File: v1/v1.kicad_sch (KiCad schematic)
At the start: 59 parts, among them CON1 SNES-CONN

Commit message: v1: fixed /WRAM vs CPU_CLK jumper selector to make sense; lots of PCB routing decisions
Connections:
- net CPU_CLK: now also JP3.3 (B); no longer JP3.2 (C)
- net ~{WRAM}: now also JP3.1 (A); no longer JP3.3 (B)
- net at Pico1.27 (GP21): now also JP3.2 (C); no longer JP3.1 (A)
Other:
- moved on the sheet: JP3
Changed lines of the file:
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@@
     (stroke (width 0) (type default) (color 0 0 0 0))
   )
+  (wire (pts (xy 189.23 151.13) (xy 186.69 151.13))
+    (stroke (width 0) (type default) (color 0 0 0 0))
+  )
   (wire (pts (xy 266.7 25.4) (xy 266.7 29.21))
     (stroke (width 0) (type default) (color 0 0 0 0))
@@
     (stroke (width 0) (type default) (color 0 0 0 0))
   )
+  (wire (pts (xy 189.23 138.43) (xy 186.69 138.43))
+    (stroke (width 0) (type default) (color 0 0 0 0))
+  )
   (wire (pts (xy 218.44 26.67) (xy 218.44 29.21))
     (stroke (width 0) (type default) (color 0 0 0 0))
@@
     (effects (font (size 1.27 1.27)) (justify right bottom))
   )
-  (label "CPU_CLK" (at 189.23 140.97 90)
+  (label "CPU_CLK" (at 189.23 138.43 0)
     (effects (font (size 1.27 1.27)) (justify left bottom))
   )
@@
     (effects (font (size 1.27 1.27)) (justify right bottom))
   )
-  (label "~{WRAM}" (at 195.58 144.78 0)
+  (label "~{WRAM}" (at 189.23 151.13 0)
     (effects (font (size 1.27 1.27)) (justify left bottom))
   )
@@
     (pin "1")
   )
-  (symbol (lib_id "Jumper:Jumper_3_Open") (at 189.23 144.78 0) (mirror x) (unit 1)
+  (symbol (lib_id "Jumper:Jumper_3_Open") (at 186.69 144.78 270) (mirror x) (unit 1)
     (in_bom yes) (on_board yes)
-    (property "Reference" "JP3" (id 0) (at 189.23 148.59 0))
-    (property "Value" "CLK_OR_WRAM" (id 1) (at 189.23 148.59 0)
+    (property "Reference" "JP3" (id 0) (at 190.5 144.78 0))
+    (property "Value" "CLK_OR_WRAM" (id 1) (at 190.5 144.78 0)
       (effects (font (size 1.27 1.27)) hide)
     )
-    (property "Footprint" "Connector_PinHeader_2.54mm:PinHeader_1x03_P2.54mm_Vertical" (id 2) (at 189.23 144.78 0)
+    (property "Footprint" "Connector_PinHeader_2.54mm:PinHeader_1x03_P2.54mm_Vertical" (id 2) (at 186.69 144.78 0)
       (effects (font (size 1.27 1.27)) hide)
     )
-    (property "Datasheet" "~" (id 3) (at 189.23 144.78 0)
+    (property "Datasheet" "~" (id 3) (at 186.69 144.78 0)
       (effects (font (size 1.27 1.27)) hide)
     )

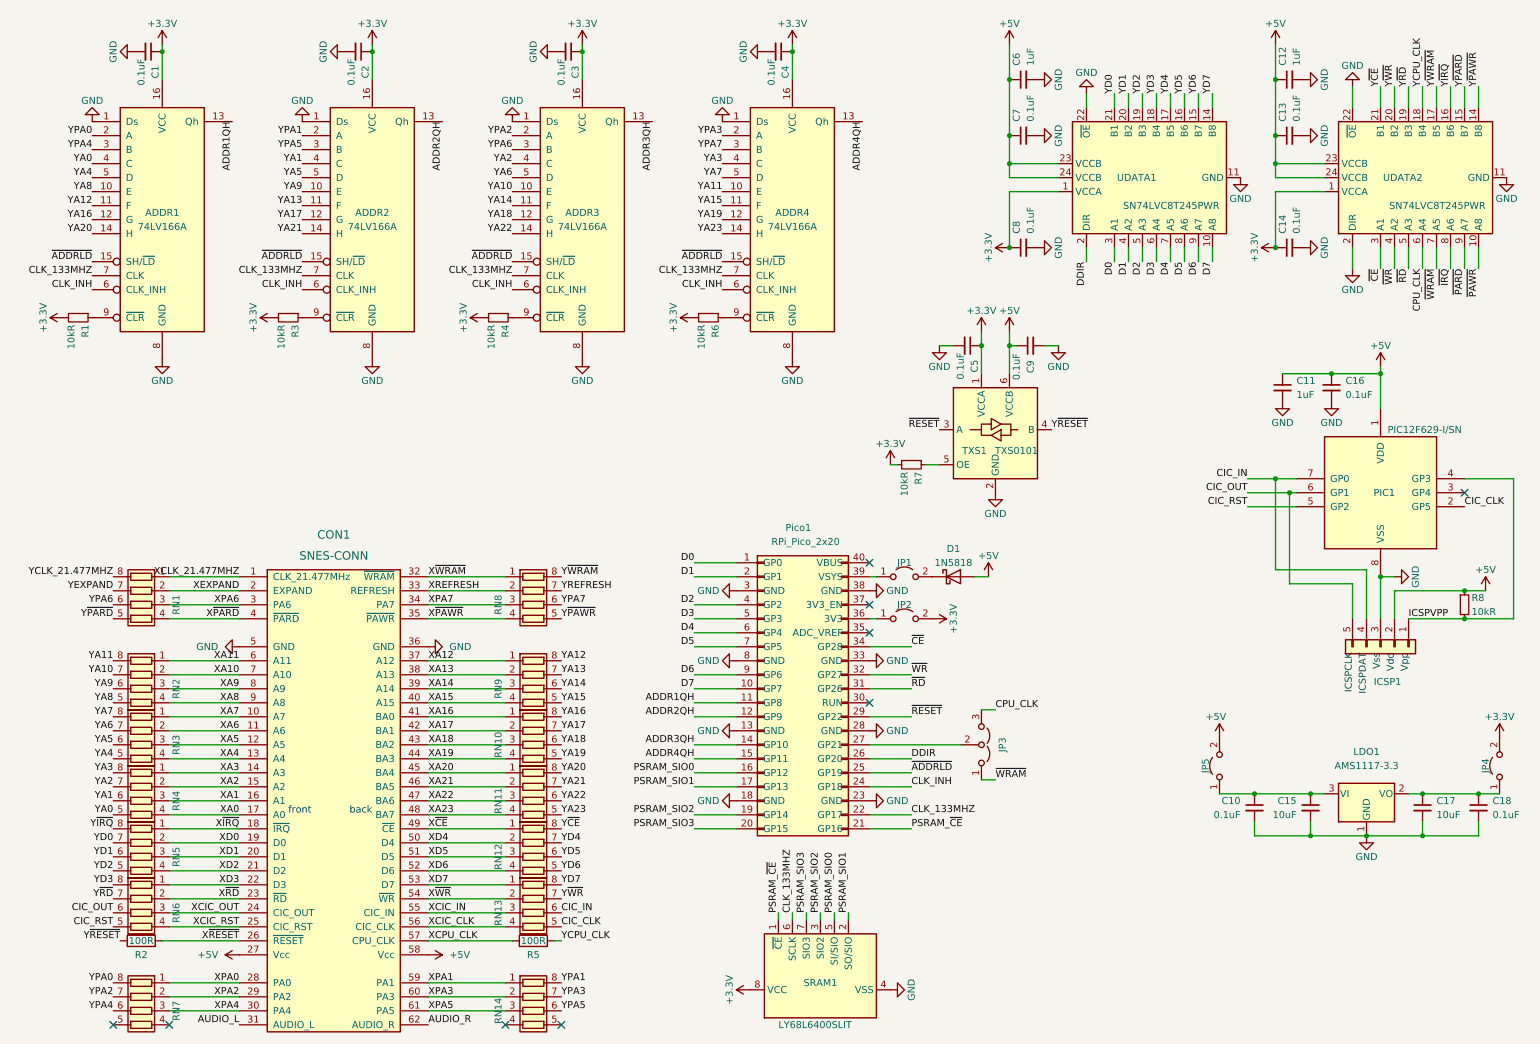
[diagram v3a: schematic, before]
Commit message: v1: lots of routing and better placement of components
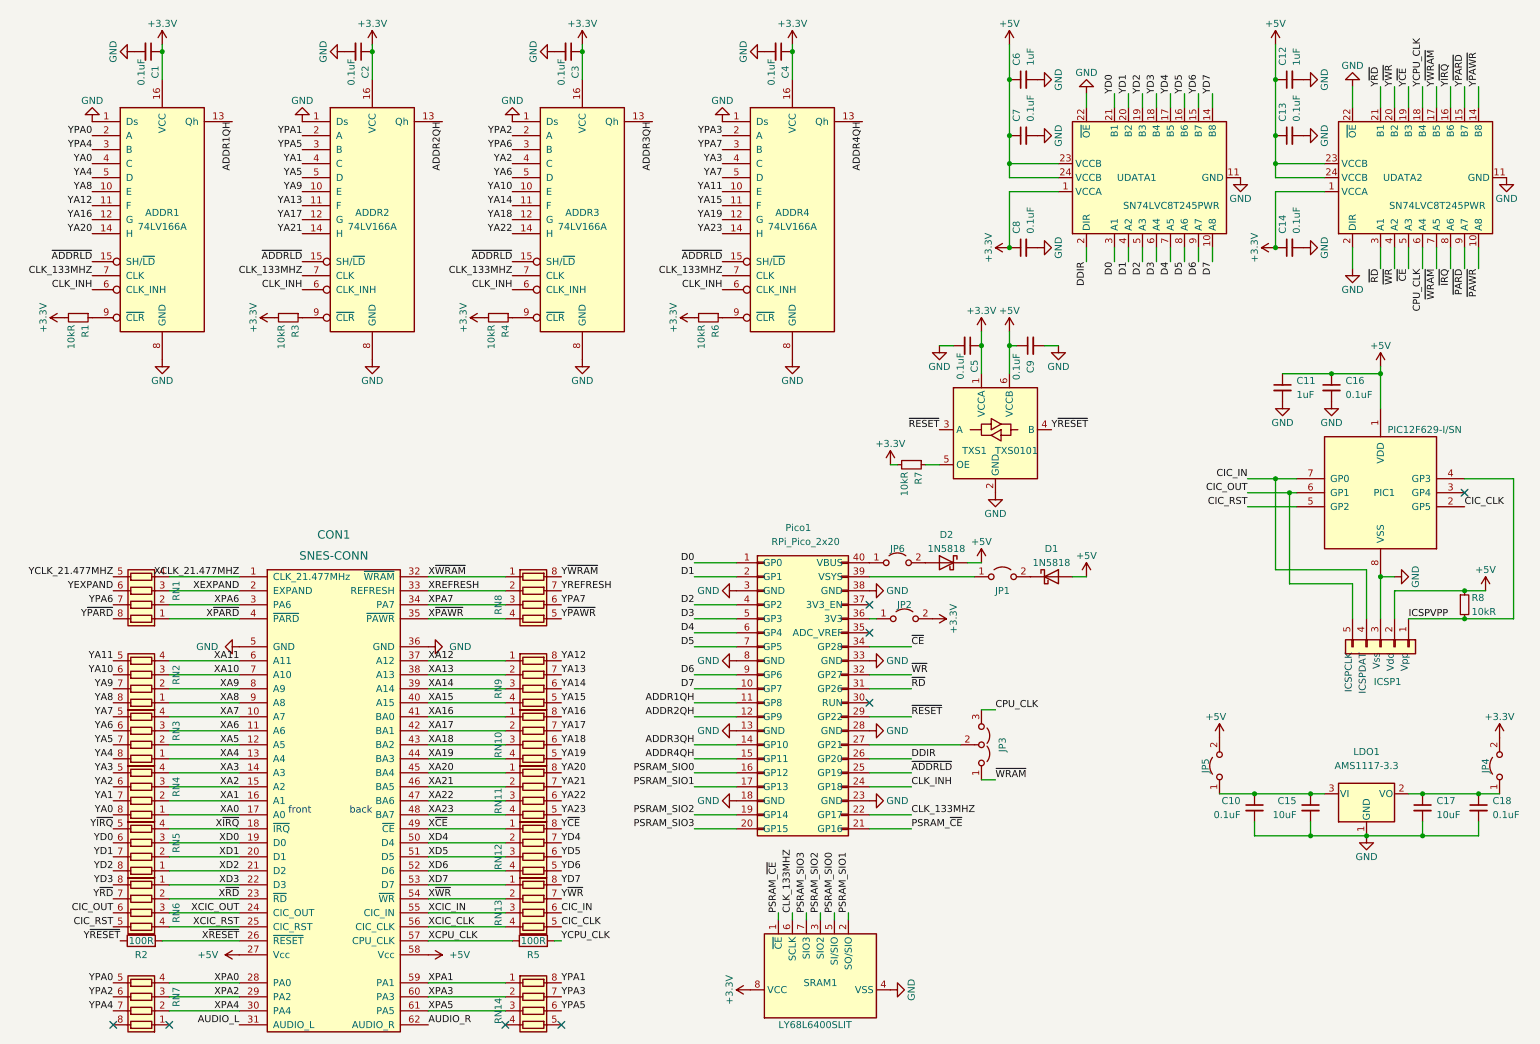
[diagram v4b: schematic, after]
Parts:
- added D2: 1N5818, Diode_THT:D_DO-41_SOD81_P7.62mm_Horizontal, symbol Diode:1N5818
- added JP6: PICO_5V_OUT, Connector_PinHeader_2.54mm:PinHeader_1x02_P2.54mm_Vertical, symbol Jumper:Jumper_2_Open
- JP1: value SNES 5V -> Pico -> PICO_5V_IN
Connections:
- net +5V: now also D2.1 (K)
- net XA0: now also RN4.1 (R1.1); no longer RN4.4 (R4.1)
- net XA1: now also RN4.2 (R2.1); no longer RN4.3 (R3.1)
- net XA10: now also RN2.3 (R3.1); no longer RN2.2 (R2.1)
- net XA11: now also RN2.4 (R4.1); no longer RN2.1 (R1.1)
- net XA2: now also RN4.3 (R3.1); no longer RN4.2 (R2.1)
- net XA3: now also RN4.4 (R4.1); no longer RN4.1 (R1.1)
- net XA4: now also RN3.1 (R1.1); no longer RN3.4 (R4.1)
- net XA5: now also RN3.2 (R2.1); no longer RN3.3 (R3.1)
- net XA6: now also RN3.3 (R3.1); no longer RN3.2 (R2.1)
- net XA7: now also RN3.4 (R4.1); no longer RN3.1 (R1.1)
- net XA8: now also RN2.1 (R1.1); no longer RN2.4 (R4.1)
- net XA9: now also RN2.2 (R2.1); no longer RN2.3 (R3.1)
- net XCLK_21.477MHZ: now also RN1.4 (R4.1); no longer RN1.1 (R1.1)
- net XD0: now also RN5.3 (R3.1); no longer RN5.2 (R2.1)
- net XD1: now also RN5.2 (R2.1); no longer RN5.3 (R3.1)
- net XD2: now also RN5.1 (R1.1); no longer RN5.4 (R4.1)
- net XEXPAND: now also RN1.3 (R3.1); no longer RN1.2 (R2.1)
- net XPA0: now also RN7.4 (R4.1); no longer RN7.1 (R1.1)
- net XPA2: now also RN7.3 (R3.1); no longer RN7.2 (R2.1)
- net XPA4: now also RN7.2 (R2.1); no longer RN7.3 (R3.1)
- net XPA6: now also RN1.2 (R2.1); no longer RN1.3 (R3.1)
- net X~{IRQ}: now also RN5.4 (R4.1); no longer RN5.1 (R1.1)
- net X~{PARD}: now also RN1.1 (R1.1); no longer RN1.4 (R4.1)
- net YA0: now also RN4.8 (R1.2); no longer RN4.5 (R4.2)
- net YA1: now also RN4.7 (R2.2); no longer RN4.6 (R3.2)
- net YA10: now also RN2.6 (R3.2); no longer RN2.7 (R2.2)
- net YA11: now also RN2.5 (R4.2); no longer RN2.8 (R1.2)
- net YA2: now also RN4.6 (R3.2); no longer RN4.7 (R2.2)
- net YA3: now also RN4.5 (R4.2); no longer RN4.8 (R1.2)
- net YA4: now also RN3.8 (R1.2); no longer RN3.5 (R4.2)
- net YA5: now also RN3.7 (R2.2); no longer RN3.6 (R3.2)
- net YA6: now also RN3.6 (R3.2); no longer RN3.7 (R2.2)
- net YA7: now also RN3.5 (R4.2); no longer RN3.8 (R1.2)
- net YA8: now also RN2.8 (R1.2); no longer RN2.5 (R4.2)
- net YA9: now also RN2.7 (R2.2); no longer RN2.6 (R3.2)
- net YCLK_21.477MHZ: now also RN1.5 (R4.2); no longer RN1.8 (R1.2)
- net YD0: now also RN5.6 (R3.2); no longer RN5.7 (R2.2)
- net YD1: now also RN5.7 (R2.2); no longer RN5.6 (R3.2)
- net YD2: now also RN5.8 (R1.2); no longer RN5.5 (R4.2)
- net YEXPAND: now also RN1.6 (R3.2); no longer RN1.7 (R2.2)
- net YPA0: now also RN7.5 (R4.2); no longer RN7.8 (R1.2)
- net YPA2: now also RN7.6 (R3.2); no longer RN7.7 (R2.2)
- net YPA4: now also RN7.7 (R2.2); no longer RN7.6 (R3.2)
- net YPA6: now also RN1.7 (R2.2); no longer RN1.6 (R3.2)
- net Y~{CE}: now also UDATA2.19 (B3); no longer UDATA2.21 (B1)
- net Y~{IRQ}: now also RN5.5 (R4.2); no longer RN5.8 (R1.2)
- net Y~{PARD}: now also RN1.8 (R1.2); no longer RN1.5 (R4.2)
- net Y~{RD}: now also UDATA2.21 (B1); no longer UDATA2.19 (B3)
- net ~{CE}: now also UDATA2.5 (A3); no longer UDATA2.3 (A1)
- net ~{RD}: now also UDATA2.3 (A1); no longer UDATA2.5 (A3)
- net at Pico1.40 (VBUS): now also JP6.1 (A)
- new net: D2.2 (A), JP6.2 (B)
- no-connect marks 9 -> 8
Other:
- moved on the sheet: D1, JP1
